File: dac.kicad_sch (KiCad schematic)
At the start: 15 parts, among them U10 TLC2272, U12 MCP4728-E_UN

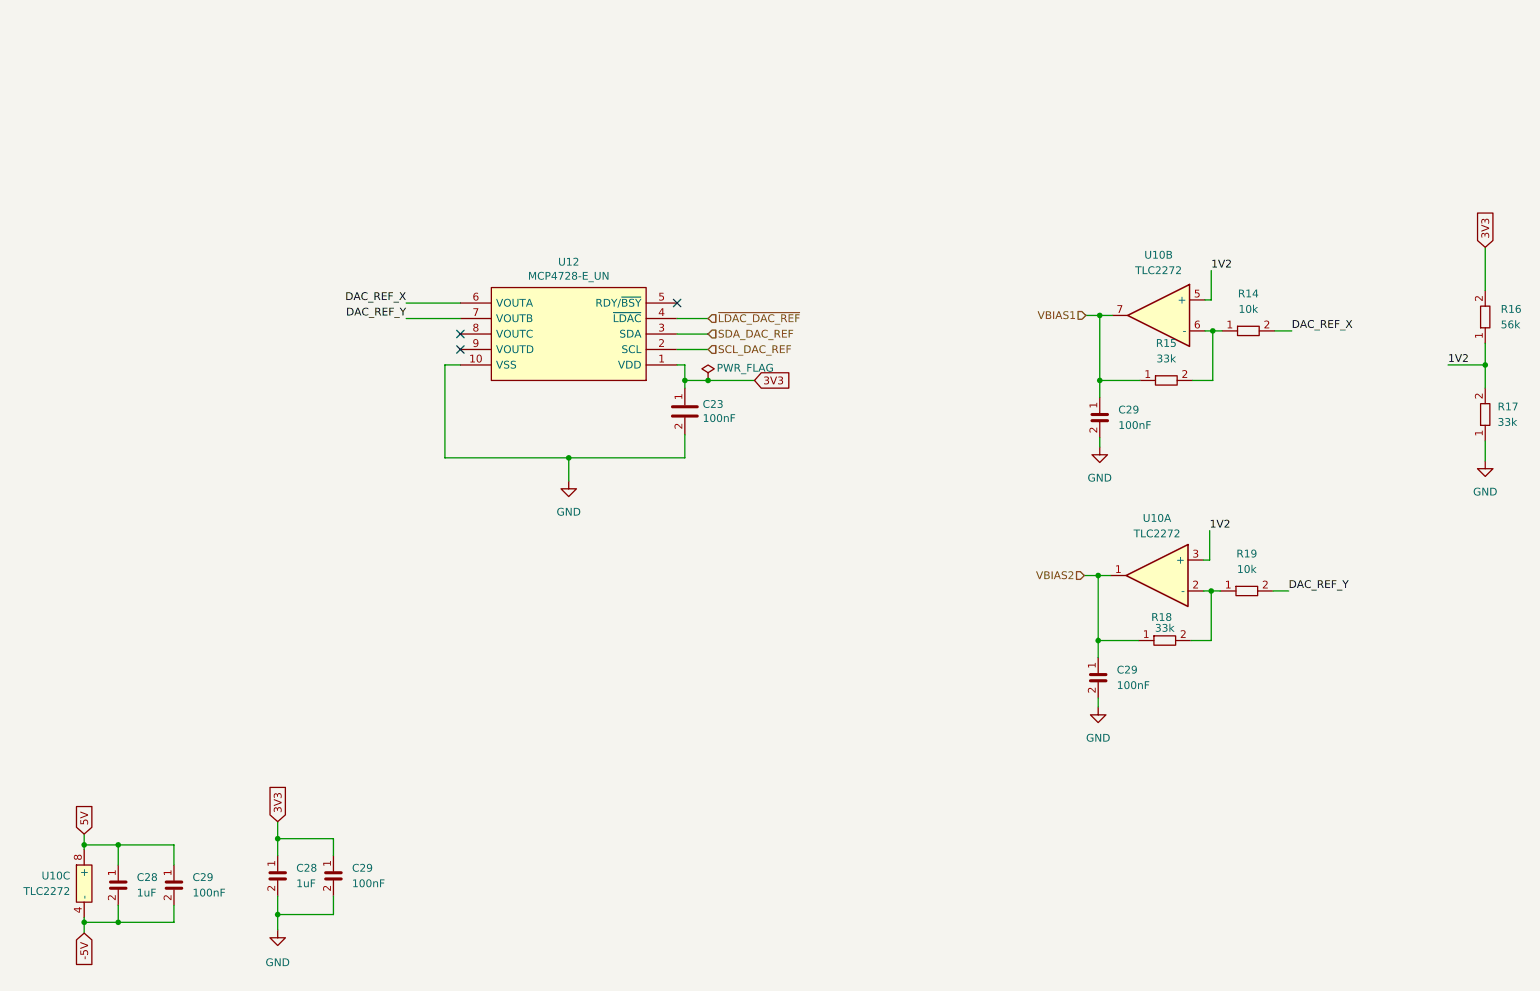
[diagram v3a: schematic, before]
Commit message: Added connector to all sheets.
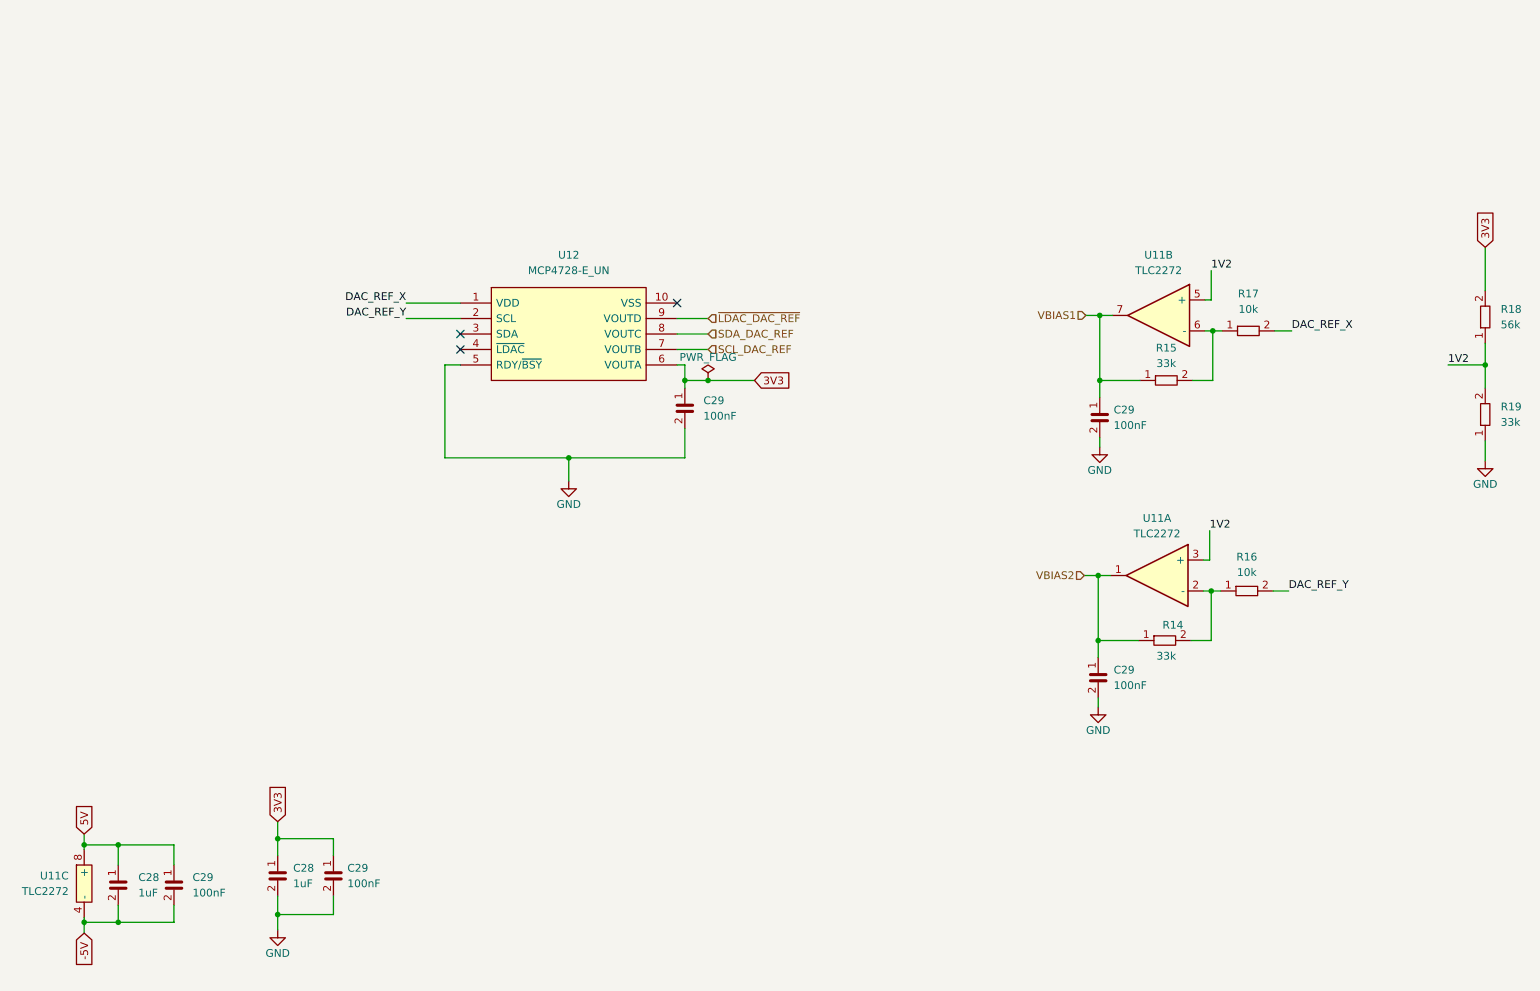
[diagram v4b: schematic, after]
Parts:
- removed C23: C0603_100nF_25V, Capacitor_SMD:C_0603_1608Metric, symbol Basis_Platine_Kompass-rescue:C0603_100nF_25V-Jojo_Kicad_Lib
- removed U12: MCP4728-E_UN, SamacSys_Parts:SOP50P490X110-10N, symbol Basis_Platine_Kompass-rescue:MCP4728-E_UN-Jojo_Kicad_Lib
- added C29: C0402_100nF_50V, Capacitor_SMD:C_0402_1005Metric, symbol Jojos_Lib:C0402_100nF_50V
- added U12: MCP4728-E_UN, Package_SO:MSOP-10_3x3mm_P0.5mm, symbol Jojos_Lib:MCP4728-E_UN
- renumbered R18 to R14, R19 to R16, R14 to R17, R16 to R18, R17 to R19, U10 to U11
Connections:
- net 3V3: now also C29.1, U12.6 (VOUTA)
- net DAC_REF_X: now also U12.1 (VDD)
- net DAC_REF_Y: now also U12.2 (SCL)
- net GND: now also C29.2, U12.5 (RDY/~{BSY})
- net SCL_DAC_REF: now also U12.7 (VOUTB)
- net SDA_DAC_REF: now also U12.8 (VOUTC)
- net ~{LDAC_DAC_REF}: now also U12.9 (VOUTD)

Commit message: Schematic finished, ready for review.
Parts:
- renumbered U12 to U10, U11 to U9
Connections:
- net 3V3: now also U10.1 (VDD); no longer U10.6 (VOUTA)
- net DAC_REF_X: now also U10.6 (VOUTA); no longer U10.1 (VDD)
- net DAC_REF_Y: now also U10.7 (VOUTB); no longer U10.2 (SCL)
- net GND: now also U10.10 (VSS); no longer U10.5 (RDY/~{BSY})
- net SCL_DAC_REF: now also U10.2 (SCL); no longer U10.7 (VOUTB)
- net SDA_DAC_REF: now also U10.3 (SDA); no longer U10.8 (VOUTC)
- net ~{LDAC_DAC_REF}: now also U10.4 (~{LDAC}); no longer U10.9 (VOUTD)
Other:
- moved on the sheet: U10

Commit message: Layout erster Entwurf fertig.
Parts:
- removed C29: C0402_100nF_50V, Capacitor_SMD:C_0402_1005Metric, symbol Jojos_Lib:C0402_100nF_50V
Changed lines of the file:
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@@
   (junction (at 30.988 171.704) (diameter 0) (color 0 0 0 0)
   )
-  (junction (at 123.952 95.504) (diameter 0) (color 0 0 0 0)
-  )
   (junction (at 255.27 92.964) (diameter 0) (color 0 0 0 0)
   )
@@
   )
   (junction (at 210.312 130.048) (diameter 0) (color 0 0 0 0)
-  )
-  (junction (at 104.902 108.204) (diameter 0) (color 0 0 0 0)
   )
   (junction (at 192.024 95.504) (diameter 0) (color 0 0 0 0)
@@
   (no_connect (at 87.122 87.884))
   (no_connect (at 87.122 90.424))
-  (wire (pts (xy 123.952 95.504) (xy 135.382 95.504))
+  (wire (pts (xy 122.682 92.964) (xy 127.762 92.964))
     (stroke (width 0) (type default))
   )
@@
     (stroke (width 0) (type default))
   )
-  (wire (pts (xy 84.582 92.964) (xy 84.582 108.204))
-    (stroke (width 0) (type default))
-  )
-  (wire (pts (xy 123.952 95.504) (xy 123.952 96.774))
-    (stroke (width 0) (type default))
-  )
-  (wire (pts (xy 122.682 92.964) (xy 123.952 92.964))
-    (stroke (width 0) (type default))
-  )
   (wire (pts (xy 220.472 130.048) (xy 223.012 130.048))
     (stroke (width 0) (type default))
@@
     (stroke (width 0) (type default))
   )
-  (wire (pts (xy 123.952 92.964) (xy 123.952 95.504))
-    (stroke (width 0) (type default))
-  )
   (wire (pts (xy 66.294 170.688) (xy 57.15 170.688))
     (stroke (width 0) (type default))
@@
     (stroke (width 0) (type default))
   )
-  (wire (pts (xy 104.902 108.204) (xy 84.582 108.204))
-    (stroke (width 0) (type default))
-  )
   (wire (pts (xy 192.024 95.504) (xy 192.024 84.836))
     (stroke (width 0) (type default))
@@
     (stroke (width 0) (type default))
   )
-  (wire (pts (xy 104.902 112.014) (xy 104.902 108.204))
+  (wire (pts (xy 86.106 92.964) (xy 86.106 95.504))
     (stroke (width 0) (type default))
   )
@@
     (stroke (width 0) (type default))
   )
-  (wire (pts (xy 123.952 108.204) (xy 104.902 108.204))
-    (stroke (width 0) (type default))
-  )
   (wire (pts (xy 122.682 90.424) (xy 127.762 90.424))
     (stroke (width 0) (type default))
@@
     (stroke (width 0) (type default))
   )
-  (wire (pts (xy 87.122 92.964) (xy 84.582 92.964))
+  (wire (pts (xy 87.122 92.964) (xy 86.106 92.964))
     (stroke (width 0) (type default))
   )
@@
   )
   (wire (pts (xy 66.294 183.134) (xy 66.294 180.086))
-    (stroke (width 0) (type default))
-  )
-  (wire (pts (xy 123.952 103.378) (xy 123.952 108.204))
     (stroke (width 0) (type default))
   )
@@
     )
   )
-  (global_label "3V3" (shape input) (at 135.382 95.504 0) (fields_autoplaced)
+  (global_label "3V3" (shape input) (at 127.762 92.964 0) (fields_autoplaced)
     (effects (font (size 1.27 1.27)) (justify left))
-    (property "Intersheetrefs" "${INTERSHEET_REFS}" (at 141.7954 95.504 0)
+    (property "Intersheetrefs" "${INTERSHEET_REFS}" (at 134.1754 92.964 0)
       (effects (font (size 1.27 1.27)) (justify left) hide)
     )
@@
     )
   )
-  (symbol (lib_id "Jojos_Lib:C0402_100nF_50V") (at 123.952 100.076 0) (unit 1)
-    (in_bom yes) (on_board yes) (dnp no) (fields_autoplaced)
-    (property "Reference" "C29" (at 127 98.806 0)
-      (effects (font (size 1.27 1.27)) (justify left))
-    )
-    (property "Value" "C0402_100nF_50V" (at 138.43 102.108 0)
-      (effects (font (size 1.27 1.27)) hide)
-    )
-    (property "Footprint" "Capacitor_SMD:C_0402_1005Metric" (at 146.558 97.79 0)
-      (effects (font (size 1.27 1.27)) hide)
-    )
-    (property "Datasheet" "" (at 123.952 100.076 0)
-      (effects (font (size 1.27 1.27)) hide)
-    )
-    (property "Mouser Part Number" "581-04025C104KAT4A" (at 140.716 100.076 0)
-      (effects (font (size 1.27 1.27)) hide)
-    )
-    (property "Place" "Yes" (at 123.952 100.076 0)
-      (effects (font (size 1.27 1.27)) hide)
-    )
-    (property "Val" "100nF" (at 127 101.346 0)
-      (effects (font (size 1.27 1.27)) (justify left))
-    )
-    (pin "1")
-    (pin "2")
-    (instances
-      (project "CMEX"
-        (path "/03c4a148-37f4-4d5a-ada3-efb0d725ba7b/006bf3bb-a88e-4438-b530-faa5a7972e5e"
-          (reference "C29") (unit 1)
-        )
-        (path "/03c4a148-37f4-4d5a-ada3-efb0d725ba7b/f0e2f768-e007-42ca-a994-5073588a4ef2"
-          (reference "C46") (unit 1)
-        )
-        (path "/03c4a148-37f4-4d5a-ada3-efb0d725ba7b/4e3d1fe0-3870-440f-98d4-103735aef720"
-          (reference "C65") (unit 1)
-        )
-      )
-    )
-  )
   (symbol (lib_id "Jojos_Lib:R0402_10k") (at 216.408 87.376 0) (unit 1)
     (in_bom yes) (on_board yes) (dnp no) (fields_autoplaced)
@@
     )
   )
-  (symbol (lib_id "power:GND") (at 104.902 112.014 0) (unit 1)
-    (in_bom yes) (on_board yes) (dnp no) (fields_autoplaced)
-    (property "Reference" "#PWR051" (at 104.902 118.364 0)
-      (effects (font (size 1.27 1.27)) hide)
-    )
-    (property "Value" "GND" (at 104.902 115.824 0)
-      (effects (font (size 1.27 1.27)))
-    )
-    (property "Footprint" "" (at 104.902 112.014 0)
-      (effects (font (size 1.27 1.27)) hide)
-    )
-    (property "Datasheet" "" (at 104.902 112.014 0)
-      (effects (font (size 1.27 1.27)) hide)
-    )
+  (symbol (lib_id "power:GND") (at 86.106 95.504 0) (unit 1)
+    (in_bom yes) (on_board yes) (dnp no) (fields_autoplaced)
+    (property "Reference" "#PWR051" (at 86.106 101.854 0)
+      (effects (font (size 1.27 1.27)) hide)
+    )
+    (property "Value" "GND" (at 86.106 99.314 0)
+      (effects (font (size 1.27 1.27)))
+    )
+    (property "Footprint" "" (at 86.106 95.504 0)
+      (effects (font (size 1.27 1.27)) hide)
+    )
+    (property "Datasheet" "" (at 86.106 95.504 0)
+      (effects (font (size 1.27 1.27)) hide)
+    )
